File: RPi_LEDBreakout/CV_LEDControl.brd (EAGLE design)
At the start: 48.2 x 25.4 mm, 7 parts, among them T1 2N2102

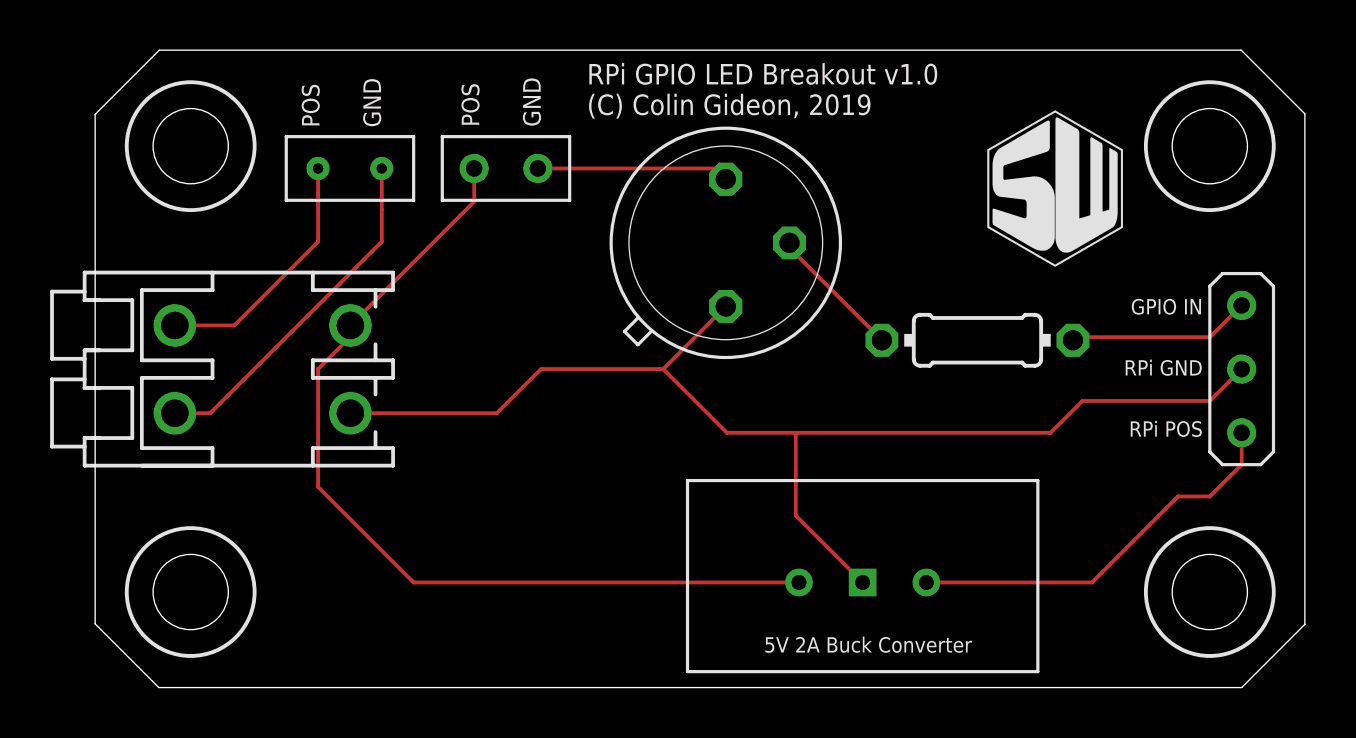
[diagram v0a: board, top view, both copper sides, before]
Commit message: Updated board design and added cleanup to end behavior
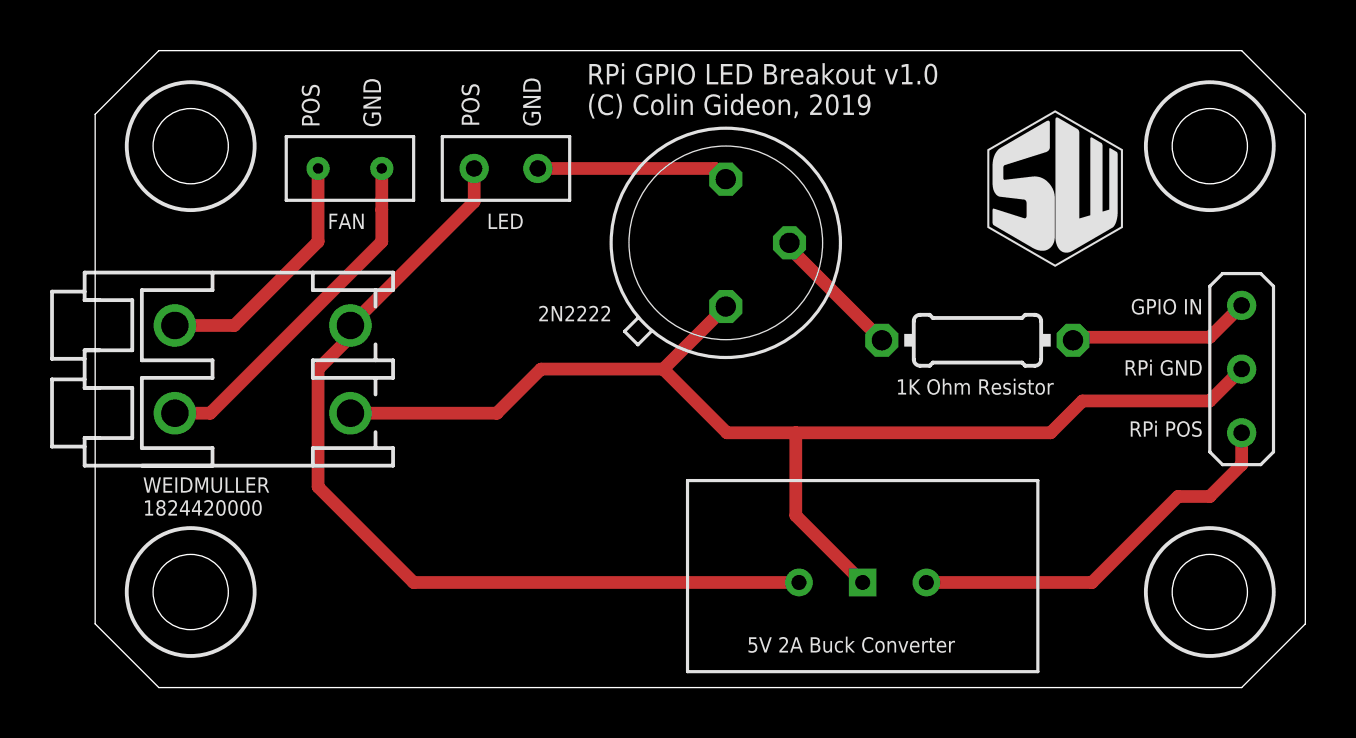
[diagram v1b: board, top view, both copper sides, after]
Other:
- board size 48.2 x 25.4 mm -> 48.3 x 25.4 mm
- board text added: "1K Ohm Resistor"
- board text added: "2N2222"
- board text added: "FAN"
- board text added: "LED"
- board text added: "WEIDMULLER 1824420000"
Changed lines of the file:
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@@
 <drawing>
 <settings>
-<setting alwaysvectorfont="yes"/>
+<setting alwaysvectorfont="no"/>
 <setting verticaltext="up"/>
 </settings>
@@
 <plain>
 <wire x1="2.54" y1="0" x2="45.72" y2="0" width="0" layer="20"/>
-<wire x1="45.72" y1="0" x2="48.24" y2="2.52" width="0" layer="20"/>
-<wire x1="48.24" y1="2.52" x2="48.24" y2="22.88" width="0" layer="20"/>
-<wire x1="48.24" y1="22.88" x2="45.701" y2="25.419" width="0" layer="20"/>
-<wire x1="45.701" y1="25.419" x2="2.559" y2="25.419" width="0" layer="20"/>
-<wire x1="2.559" y1="25.419" x2="0" y2="22.86" width="0" layer="20"/>
+<wire x1="45.72" y1="0" x2="48.26" y2="2.54" width="0" layer="20"/>
+<wire x1="48.26" y1="2.54" x2="48.26" y2="22.86" width="0" layer="20"/>
+<wire x1="48.26" y1="22.86" x2="45.72" y2="25.4" width="0" layer="20"/>
+<wire x1="45.72" y1="25.4" x2="2.54" y2="25.4" width="0" layer="20"/>
+<wire x1="2.54" y1="25.4" x2="0" y2="22.86" width="0" layer="20"/>
 <wire x1="0" y1="22.86" x2="0" y2="2.54" width="0" layer="20"/>
 <wire x1="0" y1="2.54" x2="2.54" y2="0" width="0" layer="20"/>
@@
 <circle x="44.45" y="21.59" radius="2.55" width="0.1524" layer="21"/>
 <circle x="44.45" y="3.81" radius="2.55" width="0.1524" layer="21"/>
-<text x="26.67" y="1.397" size="0.6096" layer="21">5V 2A Buck Converter</text>
+<text x="34.29" y="1.397" size="0.6096" layer="21" align="bottom-right">5V 2A Buck Converter</text>
+<text x="38.227" y="11.684" size="0.6096" layer="21" align="bottom-right">1K Ohm Resistor</text>
+<text x="17.653" y="14.605" size="0.6096" layer="21">2N2222</text>
+<text x="15.621" y="18.288" size="0.6096" layer="21">LED</text>
+<text x="9.271" y="18.288" size="0.6096" layer="21">FAN</text>
+<text x="1.905" y="6.858" size="0.6096" layer="21">WEIDMULLER
+1824420000 </text>
 </plain>
 <attributes>
@@
 <signal name="N$1">
 <contactref element="WEIDMULLERLSF" pad="A1"/>
-<wire x1="3.18" y1="14.44" x2="5.55" y2="14.44" width="0.1524" layer="1"/>
+<wire x1="3.18" y1="14.44" x2="5.55" y2="14.44" width="0.508" layer="1"/>
 <contactref element="U$2" pad="P$1"/>
-<wire x1="8.89" y1="17.78" x2="8.89" y2="20.701" width="0.1524" layer="1"/>
-<wire x1="5.55" y1="14.44" x2="8.89" y2="17.78" width="0.1524" layer="1"/>
+<wire x1="8.89" y1="17.78" x2="8.89" y2="20.701" width="0.508" layer="1"/>
+<wire x1="5.55" y1="14.44" x2="8.89" y2="17.78" width="0.508" layer="1"/>
 </signal>
 <signal name="N$2">
 <contactref element="WEIDMULLERLSF" pad="A2"/>
-<wire x1="11.43" y1="19.4564" x2="11.43" y2="19.05" width="0.1524" layer="1"/>
-<wire x1="11.43" y1="19.05" x2="11.43" y2="17.78" width="0.1524" layer="1"/>
-<wire x1="11.43" y1="17.78" x2="4.59" y2="10.94" width="0.1524" layer="1"/>
-<wire x1="4.59" y1="10.94" x2="3.18" y2="10.94" width="0.1524" layer="1"/>
+<wire x1="11.43" y1="19.4564" x2="11.43" y2="19.05" width="0.508" layer="1"/>
+<wire x1="11.43" y1="19.05" x2="11.43" y2="17.78" width="0.508" layer="1"/>
+<wire x1="11.43" y1="17.78" x2="4.59" y2="10.94" width="0.508" layer="1"/>
+<wire x1="4.59" y1="10.94" x2="3.18" y2="10.94" width="0.508" layer="1"/>
 <contactref element="U$2" pad="P$2"/>
-<wire x1="11.43" y1="19.4564" x2="11.43" y2="20.701" width="0.1524" layer="1"/>
+<wire x1="11.43" y1="19.4564" x2="11.43" y2="20.701" width="0.508" layer="1"/>
 </signal>
 <signal name="N$3">
 <contactref element="WEIDMULLERLSF" pad="A1-2"/>
 <wire x1="10.18" y1="14.44" x2="10.18" y2="13.99" width="0.1524" layer="1"/>
-<wire x1="10.18" y1="13.99" x2="8.89" y2="12.7" width="0.1524" layer="1"/>
-<wire x1="8.89" y1="12.7" x2="8.89" y2="8.001" width="0.1524" layer="1"/>
+<wire x1="10.18" y1="13.99" x2="8.89" y2="12.7" width="0.508" layer="1"/>
+<wire x1="8.89" y1="12.7" x2="8.89" y2="8.001" width="0.508" layer="1"/>
 <contactref element="U$1" pad="P$1"/>
-<wire x1="12.7" y1="4.191" x2="28.067" y2="4.191" width="0.1524" layer="1"/>
-<wire x1="8.89" y1="8.001" x2="12.7" y2="4.191" width="0.1524" layer="1"/>
+<wire x1="12.7" y1="4.191" x2="28.067" y2="4.191" width="0.508" layer="1"/>
+<wire x1="8.89" y1="8.001" x2="12.7" y2="4.191" width="0.508" layer="1"/>
 <contactref element="U$3" pad="P$1"/>
-<wire x1="15.113" y1="19.373" x2="15.113" y2="20.701" width="0.1524" layer="1"/>
-<wire x1="10.18" y1="14.44" x2="15.113" y2="19.373" width="0.1524" layer="1"/>
+<wire x1="15.113" y1="19.373" x2="15.113" y2="20.701" width="0.508" layer="1"/>
+<wire x1="10.18" y1="14.44" x2="15.113" y2="19.373" width="0.508" layer="1"/>
 </signal>
 <signal name="N$4">
 <contactref element="T1" pad="3"/>
 <contactref element="U$3" pad="P$2"/>
-<wire x1="17.653" y1="20.701" x2="24.7218" y2="20.701" width="0.1524" layer="1"/>
-<wire x1="24.7218" y1="20.701" x2="25.1484" y2="20.2744" width="0.1524" layer="1"/>
+<wire x1="17.653" y1="20.701" x2="24.7218" y2="20.701" width="0.508" layer="1"/>
+<wire x1="24.7218" y1="20.701" x2="25.1484" y2="20.2744" width="0.508" layer="1"/>
 </signal>
 <signal name="N$5">
@@
 <contactref element="U$4" pad="P$1"/>
 <wire x1="38.9942" y1="13.8496" x2="39.1146" y2="13.97" width="0.1524" layer="1"/>
-<wire x1="39.1146" y1="13.97" x2="44.45" y2="13.97" width="0.1524" layer="1"/>
-<wire x1="44.45" y1="13.97" x2="45.72" y2="15.24" width="0.1524" layer="1"/>
+<wire x1="39.1146" y1="13.97" x2="44.45" y2="13.97" width="0.508" layer="1"/>
+<wire x1="44.45" y1="13.97" x2="45.72" y2="15.24" width="0.508" layer="1"/>
 </signal>
 <signal name="N$6">
@@
 <contactref element="T1" pad="2"/>
 <wire x1="27.6884" y1="17.7344" x2="27.6884" y2="17.5354" width="0.1524" layer="1"/>
-<wire x1="27.6884" y1="17.5354" x2="31.3742" y2="13.8496" width="0.1524" layer="1"/>
+<wire x1="27.6884" y1="17.5354" x2="31.3742" y2="13.8496" width="0.508" layer="1"/>
 </signal>
 <signal name="N$8">
 <contactref element="U$1" pad="P$3"/>
-<wire x1="33.147" y1="4.191" x2="39.751" y2="4.191" width="0.1524" layer="1"/>
-<wire x1="39.751" y1="4.191" x2="43.18" y2="7.62" width="0.1524" layer="1"/>
+<wire x1="33.147" y1="4.191" x2="39.751" y2="4.191" width="0.508" layer="1"/>
+<wire x1="39.751" y1="4.191" x2="43.18" y2="7.62" width="0.508" layer="1"/>
 <contactref element="U$4" pad="P$2"/>
-<wire x1="43.18" y1="7.62" x2="44.45" y2="7.62" width="0.1524" layer="1"/>
-<wire x1="44.45" y1="7.62" x2="45.72" y2="8.89" width="0.1524" layer="1"/>
-<wire x1="45.72" y1="8.89" x2="45.72" y2="10.16" width="0.1524" layer="1"/>
+<wire x1="43.18" y1="7.62" x2="44.45" y2="7.62" width="0.508" layer="1"/>
+<wire x1="44.45" y1="7.62" x2="45.72" y2="8.89" width="0.508" layer="1"/>
+<wire x1="45.72" y1="8.89" x2="45.72" y2="10.16" width="0.508" layer="1"/>
 </signal>
 <signal name="N$7">
@@
 <contactref element="T1" pad="1"/>
 <contactref element="U$1" pad="P$2"/>
-<wire x1="10.18" y1="10.94" x2="16.02" y2="10.94" width="0.1524" layer="1"/>
-<wire x1="16.02" y1="10.94" x2="17.78" y2="12.7" width="0.1524" layer="1"/>
-<wire x1="17.78" y1="12.7" x2="22.654" y2="12.7" width="0.1524" layer="1"/>
-<wire x1="22.654" y1="12.7" x2="25.1484" y2="15.1944" width="0.1524" layer="1"/>
-<wire x1="22.654" y1="12.7" x2="25.194" y2="10.16" width="0.1524" layer="1"/>
-<wire x1="25.194" y1="10.16" x2="27.94" y2="10.16" width="0.1524" layer="1"/>
-<wire x1="38.1" y1="10.16" x2="27.94" y2="10.16" width="0.1524" layer="1"/>
-<wire x1="30.607" y1="4.191" x2="27.94" y2="6.858" width="0.1524" layer="1"/>
-<wire x1="27.94" y1="6.858" x2="27.94" y2="10.16" width="0.1524" layer="1"/>
+<wire x1="10.18" y1="10.94" x2="16.02" y2="10.94" width="0.508" layer="1"/>
+<wire x1="16.02" y1="10.94" x2="17.78" y2="12.7" width="0.508" layer="1"/>
+<wire x1="17.78" y1="12.7" x2="22.654" y2="12.7" width="0.508" layer="1"/>
+<wire x1="22.654" y1="12.7" x2="25.1484" y2="15.1944" width="0.508" layer="1"/>
+<wire x1="22.654" y1="12.7" x2="25.194" y2="10.16" width="0.508" layer="1"/>
+<wire x1="25.194" y1="10.16" x2="27.94" y2="10.16" width="0.508" layer="1"/>
+<wire x1="38.1" y1="10.16" x2="27.94" y2="10.16" width="0.508" layer="1"/>
+<wire x1="30.607" y1="4.191" x2="27.94" y2="6.858" width="0.508" layer="1"/>
+<wire x1="27.94" y1="6.858" x2="27.94" y2="10.16" width="0.508" layer="1"/>
 <contactref element="U$4" pad="P$3"/>
-<wire x1="45.72" y1="12.7" x2="44.45" y2="11.43" width="0.1524" layer="1"/>
-<wire x1="39.37" y1="11.43" x2="38.1" y2="10.16" width="0.1524" layer="1"/>
-<wire x1="44.45" y1="11.43" x2="39.37" y2="11.43" width="0.1524" layer="1"/>
+<wire x1="45.72" y1="12.7" x2="44.45" y2="11.43" width="0.508" layer="1"/>
+<wire x1="39.37" y1="11.43" x2="38.1" y2="10.16" width="0.508" layer="1"/>
+<wire x1="44.45" y1="11.43" x2="39.37" y2="11.43" width="0.508" layer="1"/>
 </signal>
 </signals>
